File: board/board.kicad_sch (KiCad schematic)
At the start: 0 parts

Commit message: board: pmic add usb
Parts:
- added C1: 1uC, symbol Device:C
- added U1: nPM1300-CAXX, nordic-lib-kicad-npm:BGA-35_7x5_3.077x2.3775mm, symbol nordic-lib-kicad-npm:nPM1300-CAXX
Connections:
- new net: U1.C1 (VSYS), U1.C2 (VSYS)
- new net: U1.D1 (VBAT), U1.D2 (VBAT)
- new net GND: C1.2, U1.A6 (VSS)
- new net cc1: U1.D5 (CC1)
- new net cc2: U1.B3 (CC2)
- new net vbus: C1.1, U1.B1 (VBUS), U1.B2 (VBUS)
- no-connect marks 0 -> 1

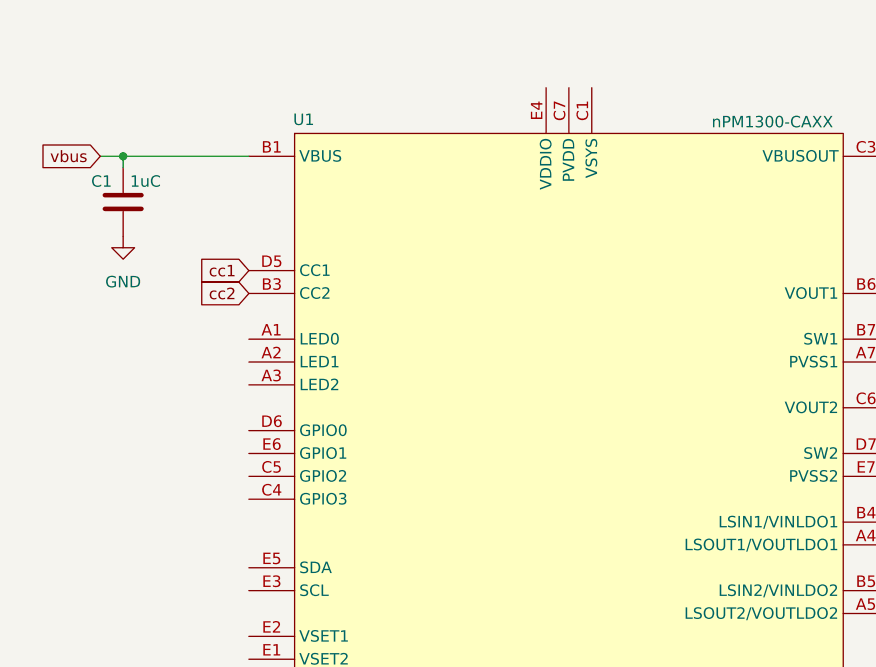
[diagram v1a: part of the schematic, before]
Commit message: board: pmic add led and gpio
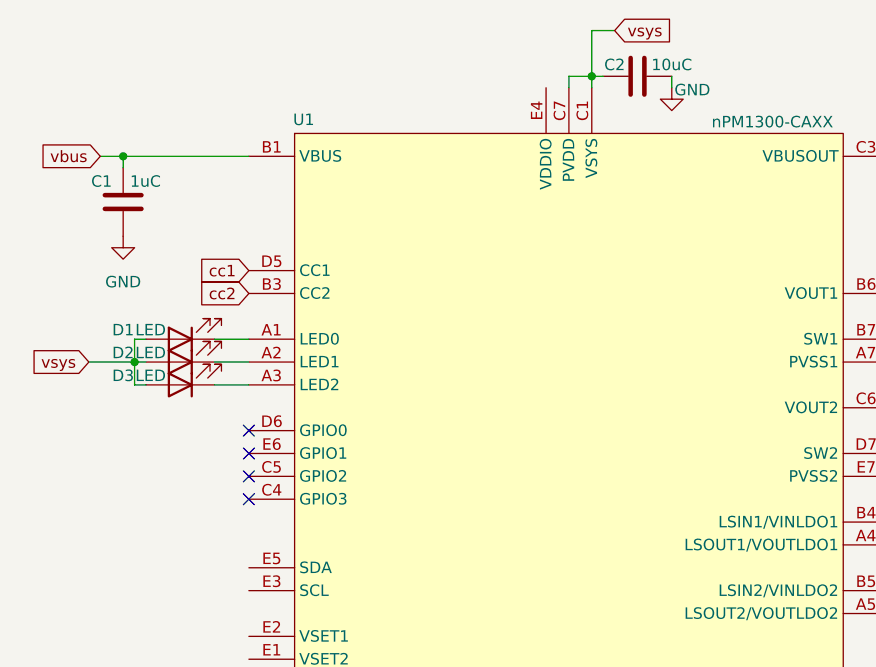
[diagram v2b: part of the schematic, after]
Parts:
- added C2: 10uC, symbol Device:C
- added D1, D2, D3: LED, symbol Device:LED
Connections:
- net GND: now also C2.2
- net at U1.A1 (LED0): now also D1.1 (K)
- net at U1.A2 (LED1): now also D2.1 (K)
- net at U1.A3 (LED2): now also D3.1 (K)
- net vsys: now reaches U1.C1 (VSYS), U1.C2 (VSYS)
- net vsys: now also U1.C7 (PVDD), C2.1, D1.2 (A), D2.2 (A), D3.2 (A)
- no-connect marks 1 -> 5

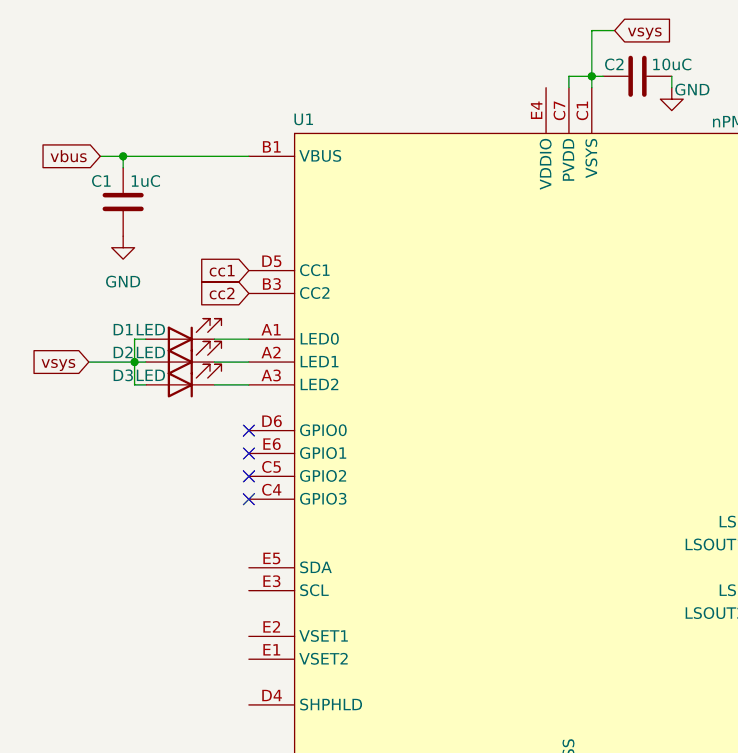
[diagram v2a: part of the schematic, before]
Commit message: board: pmic add twi
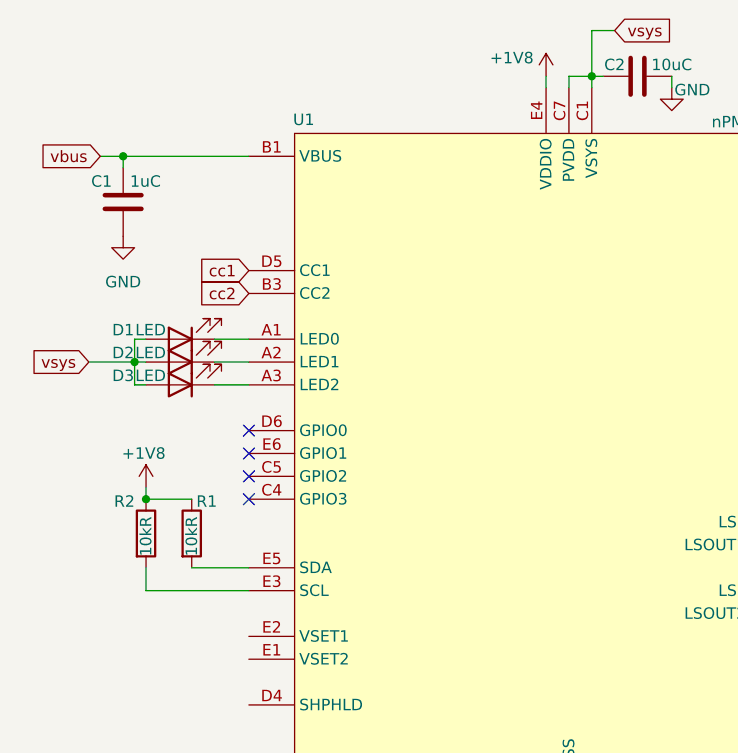
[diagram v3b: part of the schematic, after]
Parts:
- added R1, R2: 10kR, symbol Device:R
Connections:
- net at U1.E3 (SCL): now also R2.2
- net +1V8: now reaches U1.E4 (VDDIO)
- net +1V8: now also R1.1, R2.1
- net at U1.E5 (SDA): now also R1.2

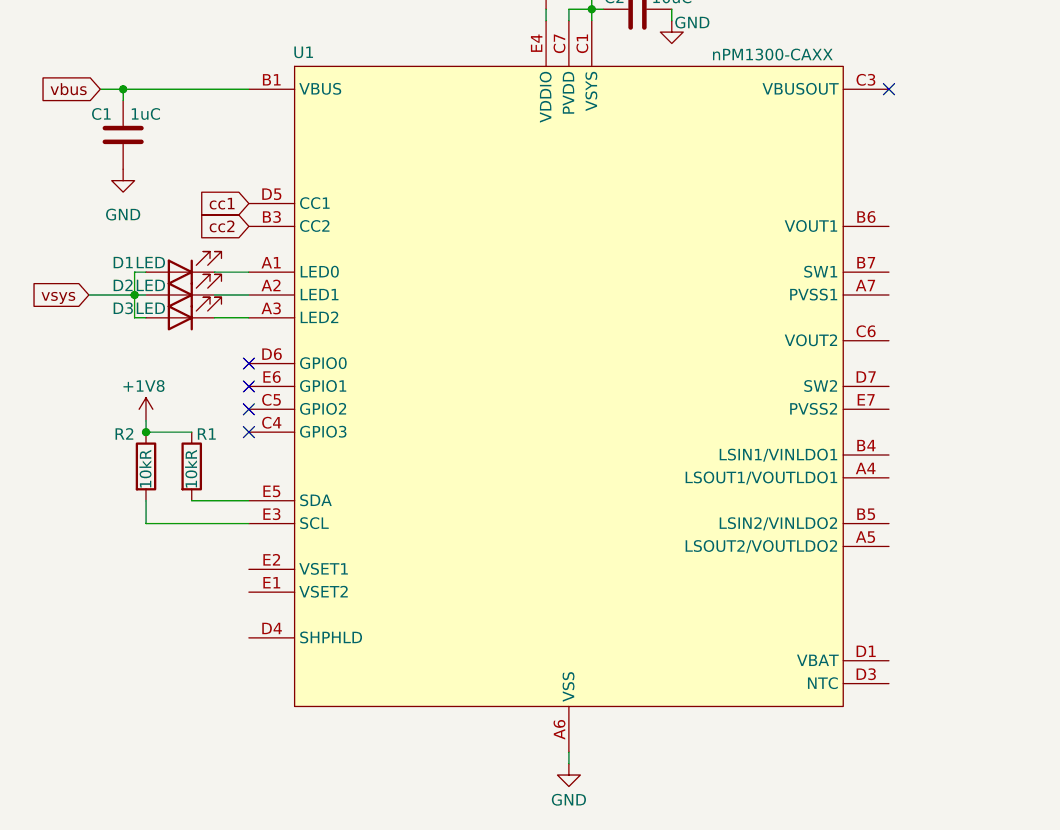
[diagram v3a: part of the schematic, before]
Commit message: baord: pmic add buck1
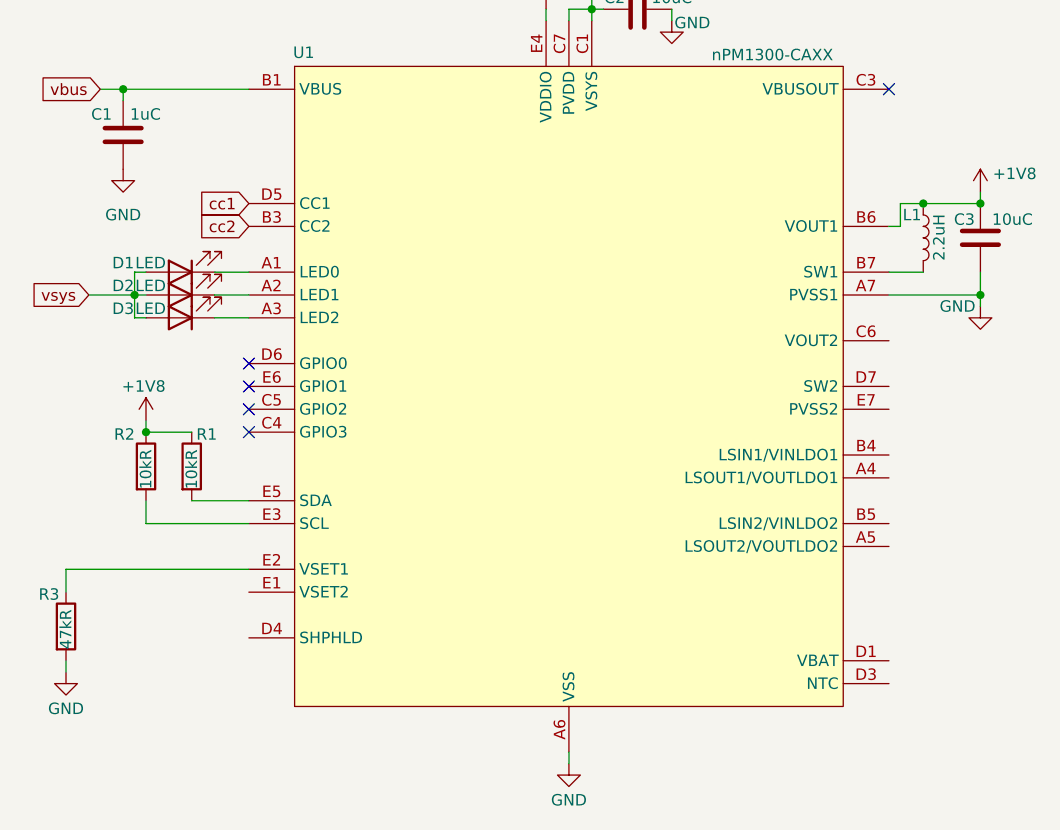
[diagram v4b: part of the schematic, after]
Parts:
- added C3: 10uC, symbol Device:C
- added L1: 2.2uH, symbol Device:L
- added R3: 47kR, symbol Device:R
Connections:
- net +1V8: now also U1.B6 (VOUT1), C3.1, L1.1
- net GND: now also U1.A7 (PVSS1), C3.2, R3.2
- net at U1.B7 (SW1): now also L1.2
- net at U1.E2 (VSET1): now also R3.1

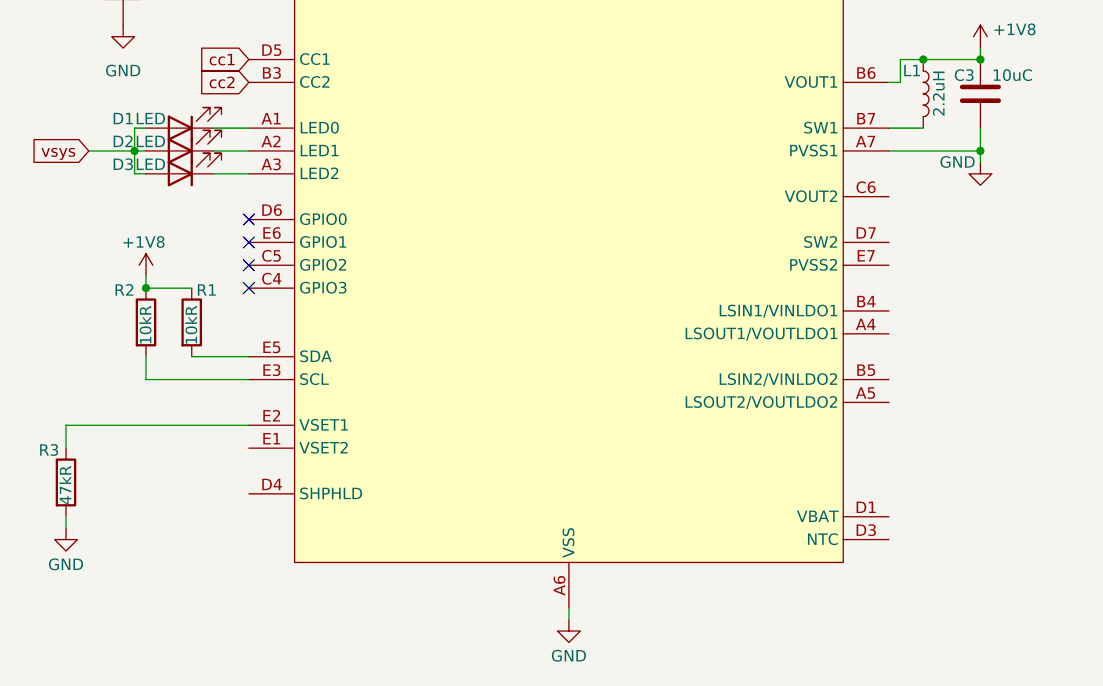
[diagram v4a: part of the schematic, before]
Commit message: board: pmic add buck2 and disable ldo1+2
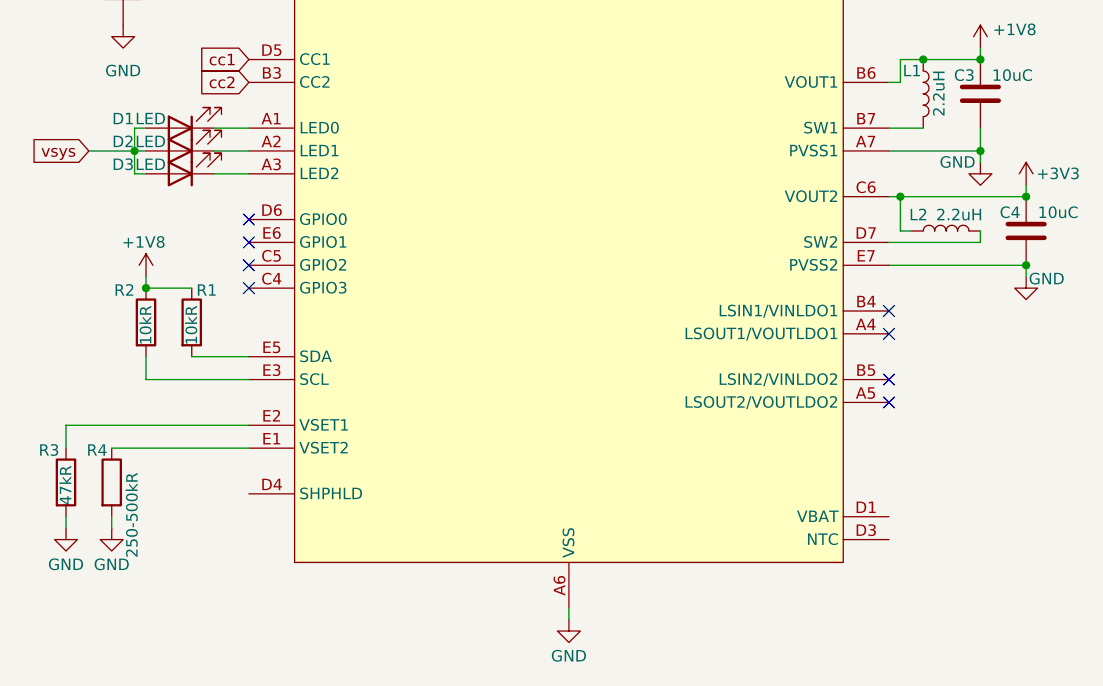
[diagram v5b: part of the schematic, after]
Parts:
- added C4: 10uC, symbol Device:C
- added L2: 2.2uH, symbol Device:L
- added R4: 250-500kR, symbol Device:R
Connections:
- net GND: now also U1.E7 (PVSS2), C4.2, R4.2
- net +3V3: now reaches U1.C6 (VOUT2)
- net +3V3: now also C4.1, L2.1
- net at U1.D7 (SW2): now also L2.2
- net at U1.E1 (VSET2): now also R4.1
- no-connect marks 5 -> 9

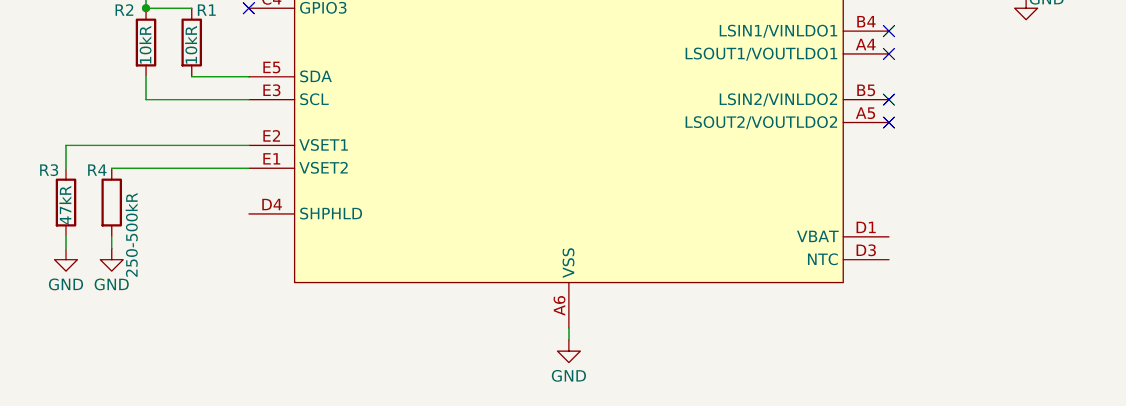
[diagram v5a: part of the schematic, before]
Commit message: board: pmic add battery management
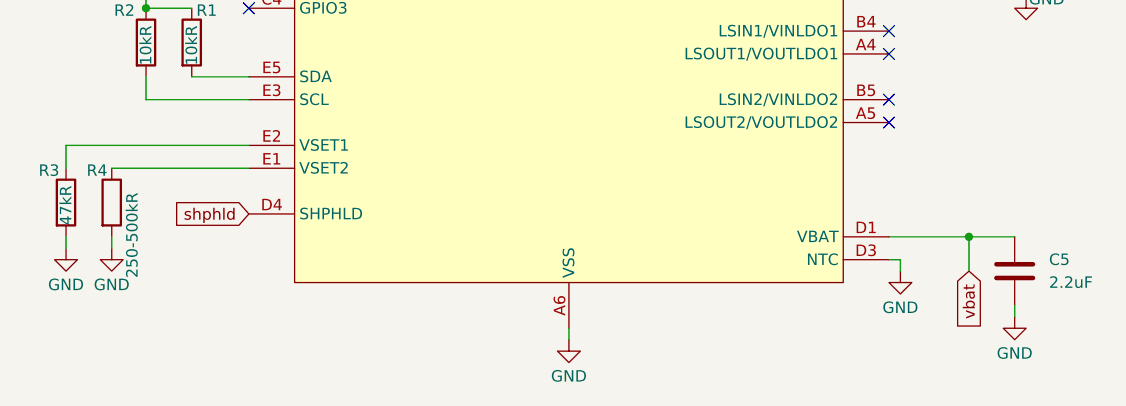
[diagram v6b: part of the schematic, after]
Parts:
- added C5: 2.2uF, symbol Device:C
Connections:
- net GND: now also U1.D3 (NTC), C5.2
- net vbat: now reaches U1.D1 (VBAT), U1.D2 (VBAT)
- net vbat: now also C5.1
- net shphld: now reaches U1.D4 (SHPHLD)

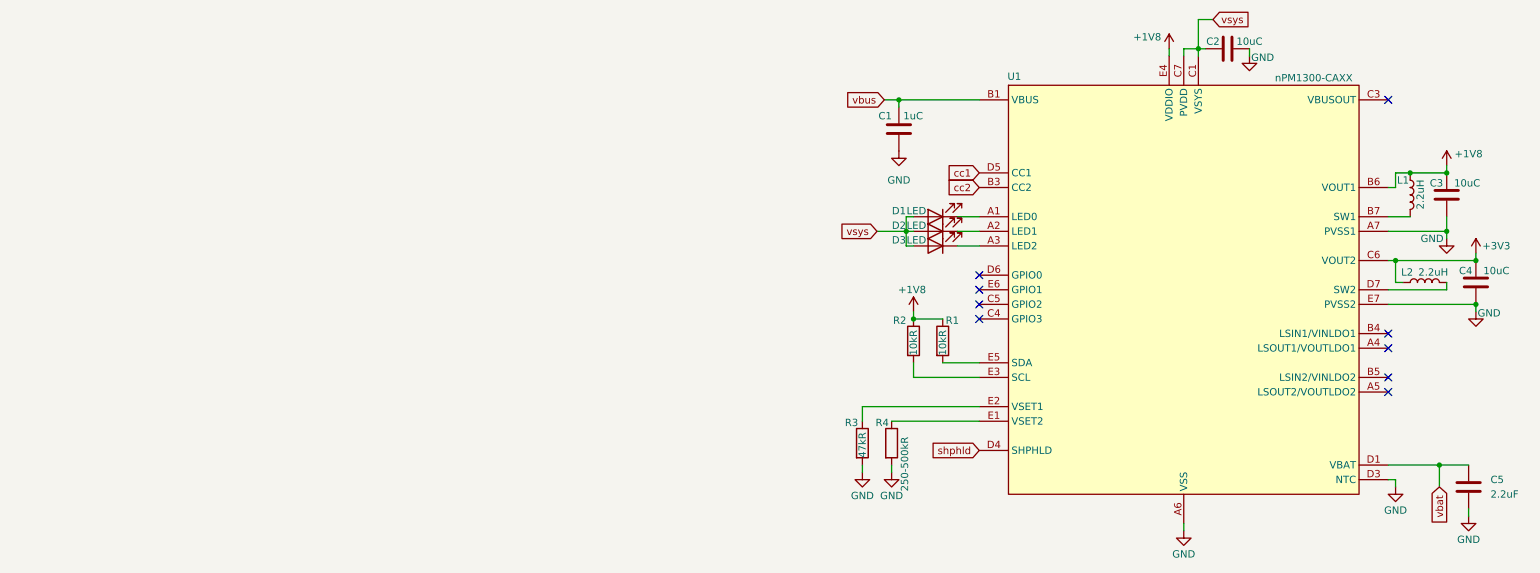
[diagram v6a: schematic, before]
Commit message: board: display add cable
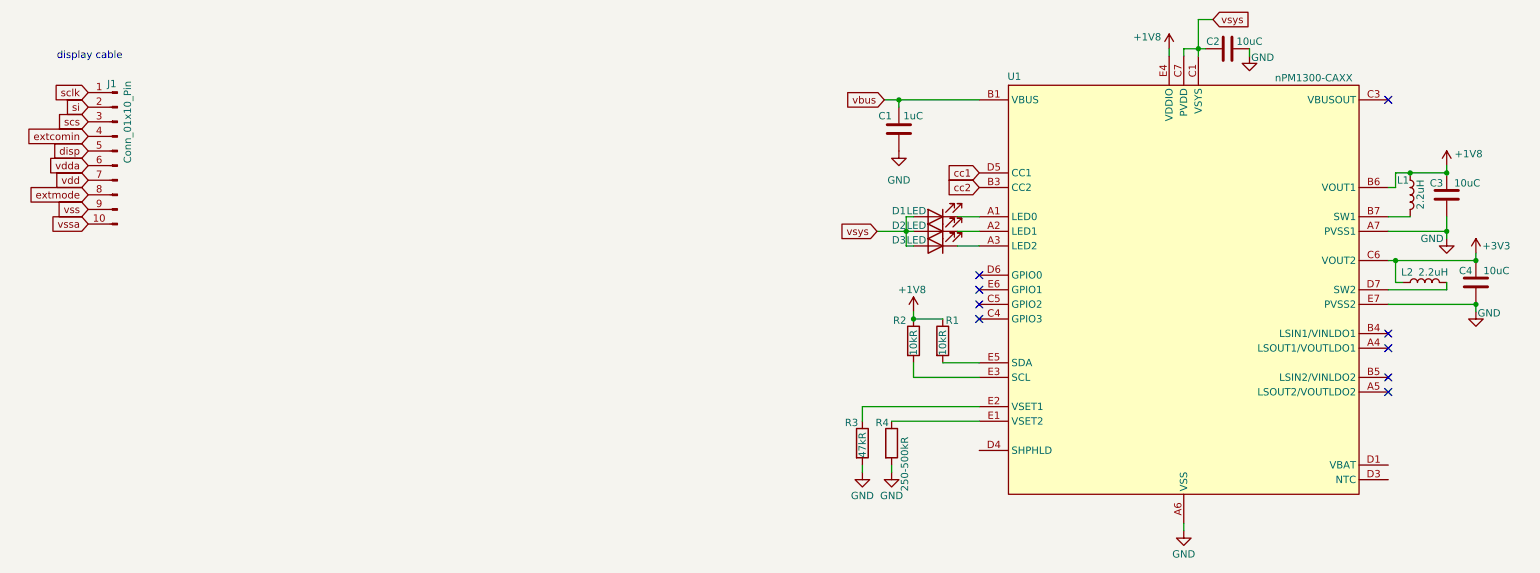
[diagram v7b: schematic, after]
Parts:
- removed C5: 2.2uF, symbol Device:C
- added J1: Conn_01x10_Pin, symbol Connector:Conn_01x10_Pin
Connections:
- net GND: no longer U1.D3 (NTC)
- net shphld: no longer names the net of U1.D4 (SHPHLD)
- net vbat: no longer names the net of U1.D1 (VBAT), U1.D2 (VBAT)
- new net disp: J1.5 (Pin_5)
- new net extcomin: J1.4 (Pin_4)
- new net extmode: J1.8 (Pin_8)
- new net sclk: J1.1 (Pin_1)
- new net scs: J1.3 (Pin_3)
- new net si: J1.2 (Pin_2)
- new net vdd: J1.7 (Pin_7)
- new net vdda: J1.6 (Pin_6)
- new net vss: J1.9 (Pin_9)
- new net vssa: J1.10 (Pin_10)
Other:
- note added: "display cable"

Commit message: board: display add power delivery net
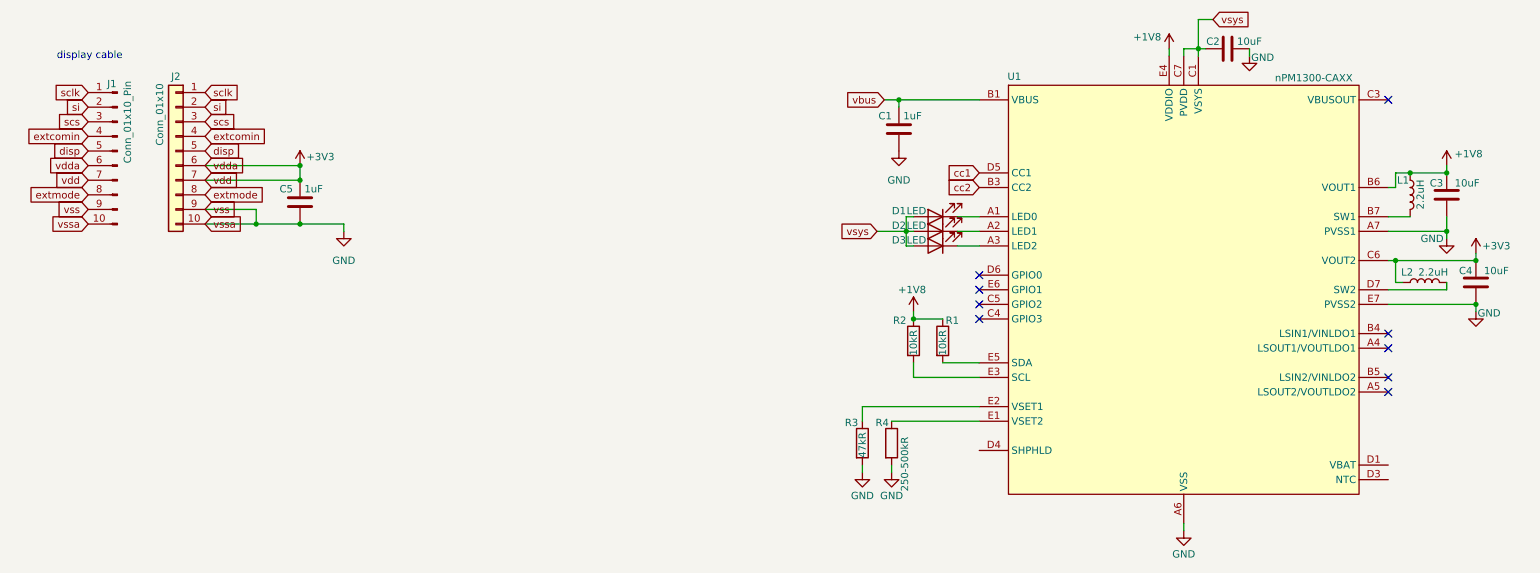
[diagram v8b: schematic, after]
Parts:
- added C5: 1uF, symbol Device:C
- added J2: Conn_01x10, symbol Connector_Generic:Conn_01x10
- C1: value 1uC -> 1uF
- C2, C3, C4: value 10uC -> 10uF
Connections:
- net vdd is gone; now on net +3V3: J1.7 (Pin_7)
- net vdda is gone; now on net +3V3: J1.6 (Pin_6)
- net vss is gone; now on net GND: J1.9 (Pin_9)
- net vssa is gone; now on net GND: J1.10 (Pin_10)
- net +3V3: now also C5.1, J2.6 (Pin_6), J2.7 (Pin_7)
- net GND: now also C5.2, J2.10 (Pin_10), J2.9 (Pin_9)
- net disp: now also J2.5 (Pin_5)
- net extcomin: now also J2.4 (Pin_4)
- net extmode: now also J2.8 (Pin_8)
- net sclk: now also J2.1 (Pin_1)
- net scs: now also J2.3 (Pin_3)
- net si: now also J2.2 (Pin_2)
